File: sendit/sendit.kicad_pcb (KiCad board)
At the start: 2 copper layers, 169 x 63.5 mm, 167 parts, among them J11 Conn_02x05_Odd_Even, J12 Conn_02x05_Odd_Even, J14 Conn_02x05_Odd_Even, J15 Conn_02x05_Odd_Even, J17 Conn_02x05_Odd_Even, J18 Conn_02x05_Odd_Even, J2 Conn_02x05_Odd_Even, J20 Conn_02x05_Odd_Even, J21 Conn_02x05_Odd_Even, J23 Conn_02x05_Odd_Even, J24 Conn_02x05_Odd_Even, J25 Micro_SD_Card, J3 Conn_02x05_Odd_Even, J5 Conn_02x05_Odd_Even, J6 Conn_02x05_Odd_Even, J8 Conn_02x05_Odd_Even, J9 Conn_02x05_Odd_Even, U2 ADS1115IDGS, U3 ADS1115IDGS, U4 TPS61040DBV

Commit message: first pass layout finished.
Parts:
- added R77: 4.7k, Resistor_SMD:R_0603_1608Metric, F.Cu at (67.2, 95.5)
- added R78: 4.7k, Resistor_SMD:R_0603_1608Metric, F.Cu at (67.2, 103.0)
- moved F2 46.1 mm to (174.6, 105.2), turned to 180 degrees
- moved TP3 42.1 mm to (171.1, 105.7)
- moved C4 42.0 mm to (179.0, 66.8)
- moved D2 42.0 mm to (175.5, 66.8)
- moved INPUT2 42.0 mm to (173.6, 117.7)
- moved J4 42.0 mm to (178.0, 110.5)
- moved J5 42.0 mm to (177.0, 97.1)
- moved J6 42.0 mm to (177.0, 74.9)
- moved R10 42.0 mm to (172.0, 88.1)
- moved R11 42.0 mm to (174.5, 89.1)
- moved R12 42.0 mm to (174.5, 86.0)
- moved R13 42.0 mm to (177.8, 89.1)
- moved R14 42.0 mm to (179.8, 89.1)
- moved R15 42.0 mm to (182.0, 89.1)
- moved R16 42.0 mm to (182.0, 86.1)
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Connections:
- H1 pad 1: unconnected-(H1-Pad1) -> GND
- H2 pad 1: unconnected-(H2-Pad1) -> GND
- H3 pad 1: unconnected-(H3-Pad1) -> GND
- H4 pad 1: unconnected-(H4-Pad1) -> GND
- U1 pad 10: CH6_A0 -> unconnected-(U1-GPIO17-Pad10)
- U1 pad 27: CH5_A1 -> unconnected-(U1-GPIO21-Pad27)
- U1 pad 28: CH5_A0 -> unconnected-(U1-GPIO47-Pad28)
- U1 pad 29: CH4_A1 -> unconnected-(U1-GPIO48-Pad29)
- U1 pad 33: CH4_A0 -> unconnected-(U1-GPIO36-Pad33)
- U1 pad 34: CH3_A1 -> unconnected-(U1-GPIO37-Pad34)
- U1 pad 36: CH3_A0 -> unconnected-(U1-GPIO39-Pad36)
- U1 pad 37: CH2_A1 -> unconnected-(U1-GPIO40-Pad37)
- U1 pad 38: CH2_A0 -> unconnected-(U1-GPIO41-Pad38)
- U1 pad 39: CH1_A1 -> unconnected-(U1-GPIO42-Pad39)
- U1 pad 40: CH1_A0 -> unconnected-(U1-GPIO2-Pad40)
- U1 pad 41: MUX_ENABLE -> unconnected-(U1-GPIO1-Pad41)
- U1 pad 5: CH8_A1 -> unconnected-(U1-GPIO5-Pad5)
- U1 pad 6: CH8_A0 -> unconnected-(U1-GPIO6-Pad6)
- U1 pad 7: CH7_A1 -> unconnected-(U1-GPIO7-Pad7)
- U1 pad 8: CH7_A0 -> unconnected-(U1-GPIO15-Pad8)
- U1 pad 9: CH6_A1 -> unconnected-(U1-GPIO16-Pad9)
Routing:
- net +3.3V: track 0.00 -> 741.9 mm, vias 0 -> 17
- net +5V: track 0.00 -> 321.4 mm, vias 0 -> 10
- net +24V: track 0.00 -> 243.1 mm, vias 0 -> 9
- net /ADC2/ADC3: track 0.00 -> 125.3 mm, vias 0 -> 2
- net /ADC2/ADC2: track 0.00 -> 111.1 mm, vias 0 -> 2
- net /ADC2/ADC1: track 0.00 -> 103.2 mm, vias 0 -> 2
- net /ADC2/ADC0: track 0.00 -> 89.5 mm, vias 0 -> 2
- net SCL: track 0.00 -> 80.8 mm, vias 0 -> 2
- net SD_CS: track 0.00 -> 79.5 mm, vias 0 -> 2
- net SDA: track 0.00 -> 73.9 mm, vias 0 -> 3
- net MOSI: track 0.00 -> 72.7 mm, vias 0 -> 2
- net GND: track 0.00 -> 69.1 mm, vias 0 -> 55
- net /ADC1/ADC3: track 0.00 -> 65.2 mm, vias 0 -> 2
- net MISO: track 0.00 -> 61.7 mm, vias 0 -> 2
- net CLK: track 0.00 -> 58.3 mm, vias 0 -> 2
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- added copper zone on B.Cu, net GND
- added copper zone on F.Cu, net GND
- added copper zone on In1.Cu, net GND
- added copper zone on In2.Cu, net GND
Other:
- board size 169 x 63.5 mm -> 169 x 66 mm
- copper layers 2 -> 4
- board text added: "24V"
- board text added: "3V3"
- board text added: "5V0"

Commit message: finished layout and routing
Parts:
- added LOGO1: ~, yarrboard:Logo Small, F.Cu at (82.8, 77.6)
- added LOGO2: Logo_Open_Hardware_Small, Symbol:OSHW-Logo_5.7x6mm_SilkScreen, F.Cu at (228.8, 110.2)
- moved R77 1.41 mm to (68.2, 94.5), turned to 90 degrees
- moved R78 1.25 mm to (68.2, 102.2), turned to 90 degrees
- moved H1 0.71 mm to (66.5, 63.5)
- moved H2 0.71 mm to (228.5, 63.5)
- moved H3 0.71 mm to (228.5, 122.5)
- moved H4 0.71 mm to (66.5, 122.5)
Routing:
- net +3.3V: track 741.9 -> 739.6 mm
- net SDA: track 73.9 -> 72.4 mm
- net SCL: track 80.8 -> 79.9 mm
- net /ADC2/ADC0: track 89.5 -> 88.8 mm
- net MOSI: track 72.7 -> 72.1 mm
- net /ADC2/ADC1: track 103.2 -> 103.7 mm
- net GND: vias 55 -> 52
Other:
- board text added: "CH1"
- board text added: "CH2"
- board text added: "CH3"
- board text added: "CH4"
- board text added: "CH5"
- board text added: "CH6"
- board text added: "CH7"
- board text added: "CH8"
- board text added: "SendIt Rev A"
- board text added: "YARRBOARD"
- board text added: "https://github.com/hoeken/sendit"

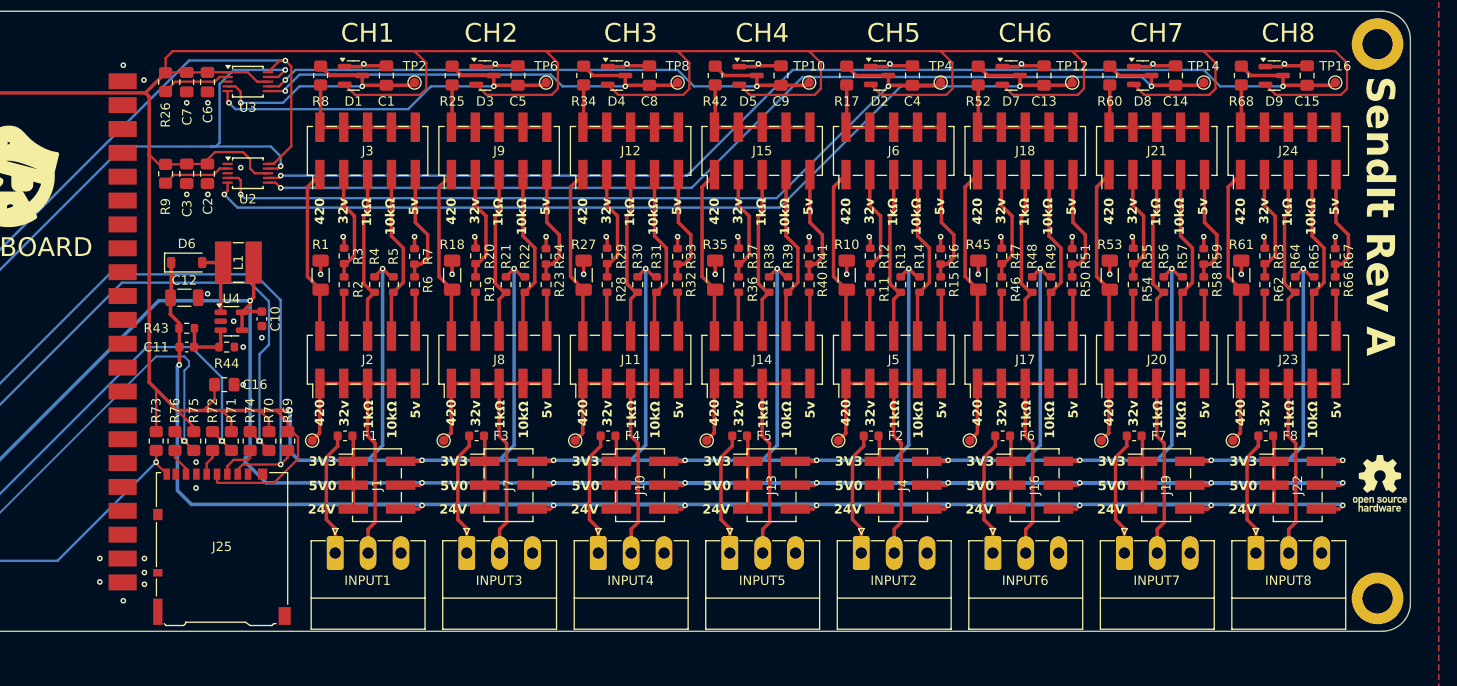
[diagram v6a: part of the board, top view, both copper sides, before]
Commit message: updated footprints and lcsc numbers.
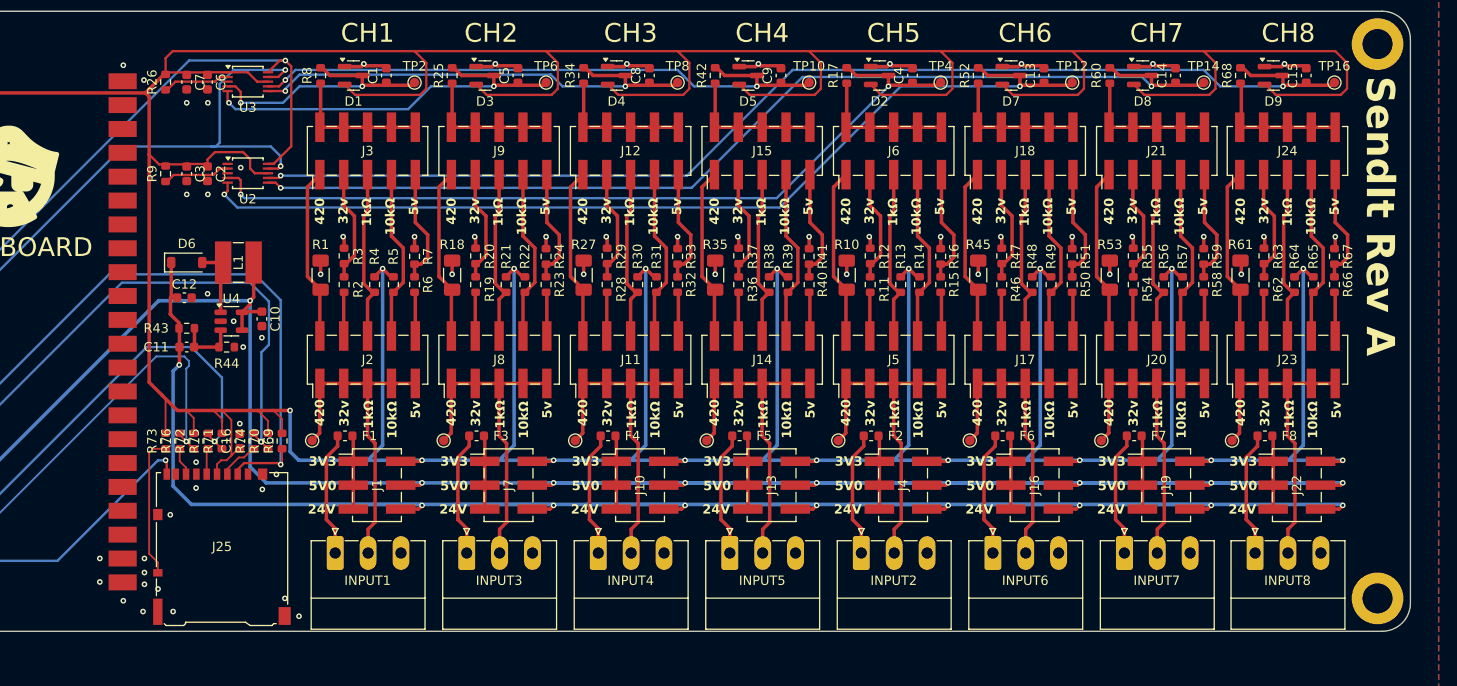
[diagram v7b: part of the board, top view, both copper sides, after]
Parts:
- removed LOGO2: Logo_Open_Hardware_Small, Symbol:OSHW-Logo_5.7x6mm_SilkScreen
- C1, C13, C14, C15, C16, C2, C3, C4, C5, C6, C7, C8, C9: footprint Capacitor_SMD:C_0805_2012Metric_Pad1.18x1.45mm_HandSolder -> Capacitor_SMD:C_0603_1608Metric
- C12: footprint Capacitor_SMD:C_1206_3216Metric -> Capacitor_SMD:C_0603_1608Metric
- R13, R21, R30, R38, R4, R48, R56, R64: value 1k 0.1% -> 1k 1%
- R15, R23, R32, R40, R50, R58, R6, R66: value 470 0.1% -> 560 0.1%
- R16, R24, R33, R41, R51, R59, R67, R7: value 910 0.1% -> 1k 0.1%
- R17, R25, R26, R34, R42, R52, R60, R68, R69, R70, R71, R72, R74, R75, R76, R8, R9: footprint Resistor_SMD:R_0805_2012Metric_Pad1.20x1.40mm_HandSolder -> Resistor_SMD:R_0603_1608Metric
- R73: value 10k -> 4.7k; footprint Resistor_SMD:R_0805_2012Metric_Pad1.20x1.40mm_HandSolder -> Resistor_SMD:R_0603_1608Metric
- moved C16 6.22 mm to (107.4, 105.8), turned to 90 degrees
- moved R71 1.00 mm to (105.5, 105.8)
- moved R73 1.00 mm to (99.5, 105.8)
- moved R69 0.60 mm to (111.9, 105.8)
- moved R75 0.50 mm to (104.0, 105.8)
- moved R76 0.50 mm to (101.0, 105.8)
- moved R74 0.40 mm to (108.9, 105.8)
- moved R70 0.10 mm to (110.4, 105.8)
- moved INPUT8 0.09 mm to (215.5, 117.7)
- moved C15 0.09 mm to (220.9, 66.8)
- moved D9 0.09 mm to (217.4, 66.8)
- moved F8 0.09 mm to (216.5, 105.2)
- moved J22 0.09 mm to (219.9, 110.5)
- moved J23 0.09 mm to (218.9, 97.1)
- moved J24 0.09 mm to (218.9, 74.9)
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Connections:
- J25 pad 10: GND -> Net-(J25-DET_A)
- J25 pad 11: (no net) -> GND
- R73 pad 1: SD_DETECT -> Net-(J25-DET_A)
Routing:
- net Net-(J25-DET_A): track 0.00 -> 15.1 mm
- net +3.3V: track 739.6 -> 731.1 mm
- net MISO: track 61.4 -> 60.8 mm
- net MOSI: track 72.1 -> 71.5 mm
- net GND: track 69.1 -> 69.3 mm, vias 52 -> 60

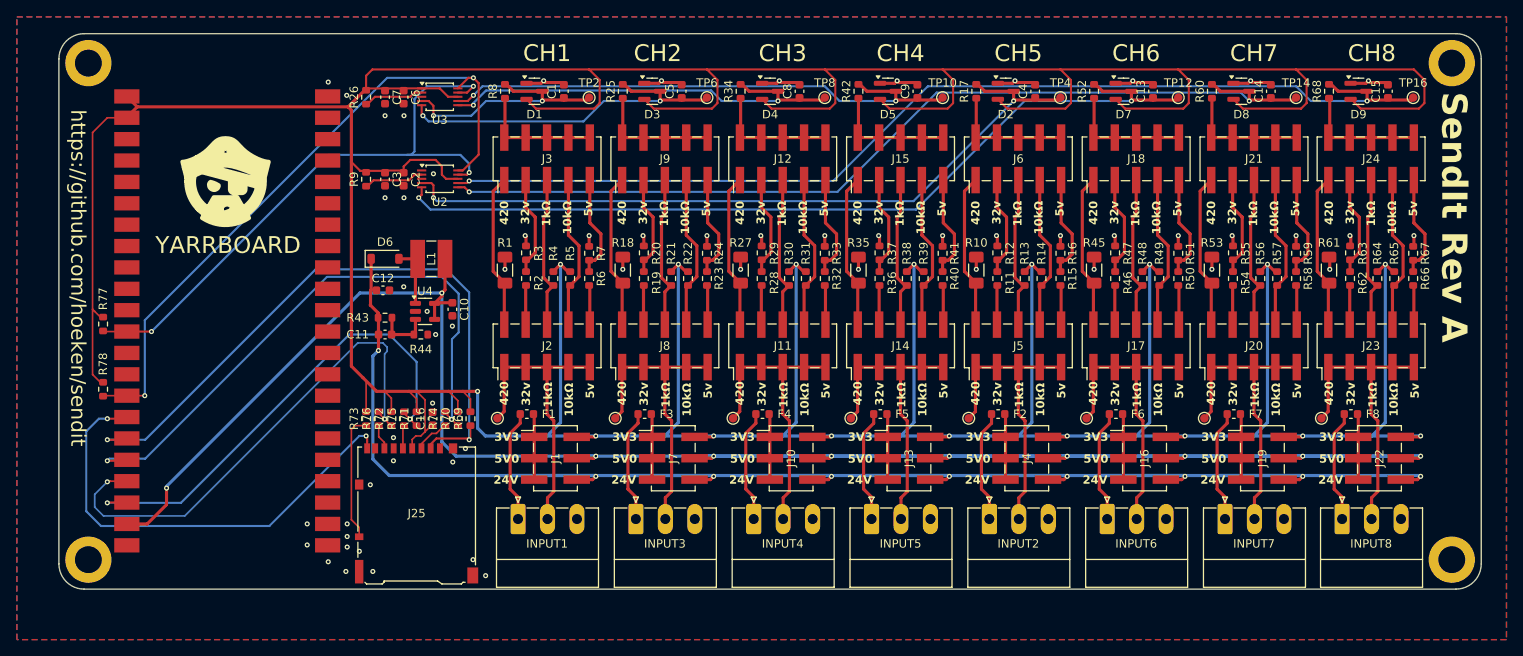
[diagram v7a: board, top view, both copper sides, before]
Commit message: added fuses, 24v filters, and indicator leds.
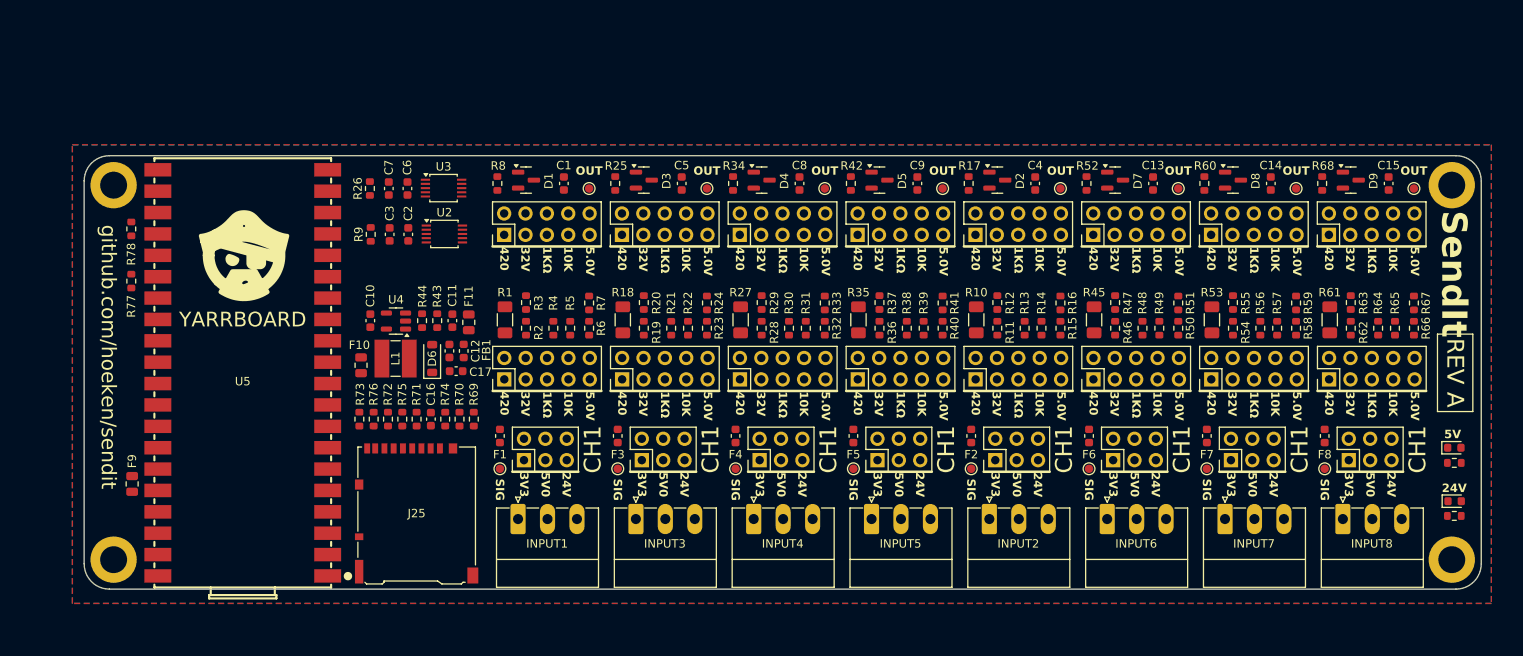
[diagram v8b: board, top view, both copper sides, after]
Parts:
- removed U1: ~, yarrboard:Waveshare-ESP32-S3-dev-kit-SMD
- added C17: 1uF, Capacitor_SMD:C_0603_1608Metric, F.Cu at (110.2, 100.1)
- added D10: PWR, LED_SMD:LED_0603_1608Metric, F.Cu at (228.8, 115.5)
- added D19: PWR, LED_SMD:LED_0603_1608Metric, F.Cu at (228.8, 109.2)
- added F10: 200mA, Fuse:Fuse_0805_2012Metric, F.Cu at (98.9, 99.4)
- added F11: 300mA / 30v, Fuse:Fuse_0805_2012Metric, F.Cu at (111.7, 94.3)
- added F9: 750mA, Fuse:Fuse_0805_2012Metric, F.Cu at (71.7, 113.5)
- added FB1: BLM18EG101TN1D, Inductor_SMD:L_0603_1608Metric, F.Cu at (111.1, 97.7)
- added R79: 5.6k, Resistor_SMD:R_0603_1608Metric, F.Cu at (228.8, 117.3)
- added R80: 560, Resistor_SMD:R_0603_1608Metric, F.Cu at (228.8, 111.0)
- added U5: ~, yarrboard:ESP32-S3-PICO, F.Cu at (84.8, 101.3)
- J1, J10, J13, J16, J19, J22, J4, J7: footprint Connector_PinHeader_2.54mm:PinHeader_2x03_P2.54mm_Vertical_SMD -> Connector_PinHeader_2.54mm:PinHeader_2x03_P2.54mm_Vertical
- J11, J12, J14, J15, J17, J18, J2, J20, J21, J23, J24, J3, J5, J6, J8, J9: footprint Connector_PinHeader_2.54mm:PinHeader_2x05_P2.54mm_Vertical_SMD -> Connector_PinHeader_2.54mm:PinHeader_2x05_P2.54mm_Vertical
- moved R78 19.3 mm to (71.6, 83.2)
- moved H1 14.8 mm to (69.5, 78.0)
- moved H2 14.5 mm to (228.5, 78.0)
- moved D6 13.1 mm to (107.3, 98.6), turned to 90 degrees
- moved L1 12.6 mm to (103.0, 98.6), turned to 0 degrees
- moved R17 11.0 mm to (171.1, 77.8)
- moved R25 11.0 mm to (129.1, 77.8)
- moved R34 11.0 mm to (143.1, 77.8)
- moved R42 11.0 mm to (157.1, 77.8)
- moved R52 11.0 mm to (185.1, 77.8)
- moved R60 11.0 mm to (199.1, 77.8)
- moved R8 11.0 mm to (115.1, 77.8)
- moved R68 11.0 mm to (213.1, 77.8)
- moved C15 11.0 mm to (221.0, 77.8)
- moved C1 11.0 mm to (123.0, 77.8)
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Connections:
- C11 pad 1: +24V -> Net-(D6-K)
- C12 pad 1: +24V -> Net-(C12-Pad1)
- D6 pad 1: +24V -> Net-(D6-K)
- R43 pad 1: +24V -> Net-(D6-K)
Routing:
- net +3.3V: track 731.1 -> 0.00 mm, vias 17 -> 0
- net +5V: track 321.0 -> 0.00 mm, vias 10 -> 0
- net +24V: track 243.6 -> 0.00 mm, vias 9 -> 0
- net /ADC2/ADC3: track 125.2 -> 0.00 mm, vias 2 -> 0
- net /ADC2/ADC2: track 111.3 -> 0.00 mm, vias 2 -> 0
- net /ADC2/ADC1: track 103.7 -> 0.00 mm, vias 2 -> 0
- net /ADC2/ADC0: track 88.8 -> 0.00 mm, vias 2 -> 0
- net SCL: track 79.9 -> 0.00 mm, vias 2 -> 0
- net SD_CS: track 79.6 -> 0.00 mm, vias 2 -> 0
- net SDA: track 72.4 -> 0.00 mm, vias 3 -> 0
- net MOSI: track 71.5 -> 0.00 mm, vias 2 -> 0
- net GND: track 69.3 -> 0.00 mm, vias 60 -> 0
- net /ADC1/ADC3: track 65.2 -> 0.00 mm, vias 2 -> 0
- net MISO: track 60.8 -> 0.00 mm, vias 2 -> 0
- net CLK: track 58.1 -> 0.00 mm, vias 2 -> 0
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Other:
- board size 169 x 66 mm -> 166 x 51.5 mm
- board text added: "10K"
- board text added: "1KΩ"
- board text added: "32V"
- board text added: "5.0V"
- board text added: "5V"
- board text added: "OUT"
- board text added: "REV A"
- board text added: "SIG"
- board text added: "SendIt"
- board text added: "github.com/hoeken/sendit"
- board text removed: "10kΩ"
- board text removed: "1kΩ"
- board text removed: "32v"
- board text removed: "5v"
- board text removed: "CH2"
- board text removed: "CH3"
- board text removed: "CH4"
- board text removed: "CH5"
- board text removed: "CH6"
- board text removed: "CH7"
- board text removed: "CH8"
- board text removed: "SendIt Rev A"
- board text removed: "https://github.com/hoeken/sendit"
